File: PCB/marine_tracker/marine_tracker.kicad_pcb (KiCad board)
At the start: 4 copper layers, 83.7 x 40.3 mm, 59 parts, among them J1 Screw_Terminal_01x02, J2 Conn_ARM_JTAG_SWD_10, J3 USB_C_Receptacle_USB2.0_16P, J4 BM04B-GHS-TBT, J5 Conn_01x08_Pin, J6 Conn_Coaxial, SW1 SW_Push, U1 STM32U575RGT6, U2 SHT40, U3 MCP73833-xxx-UN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

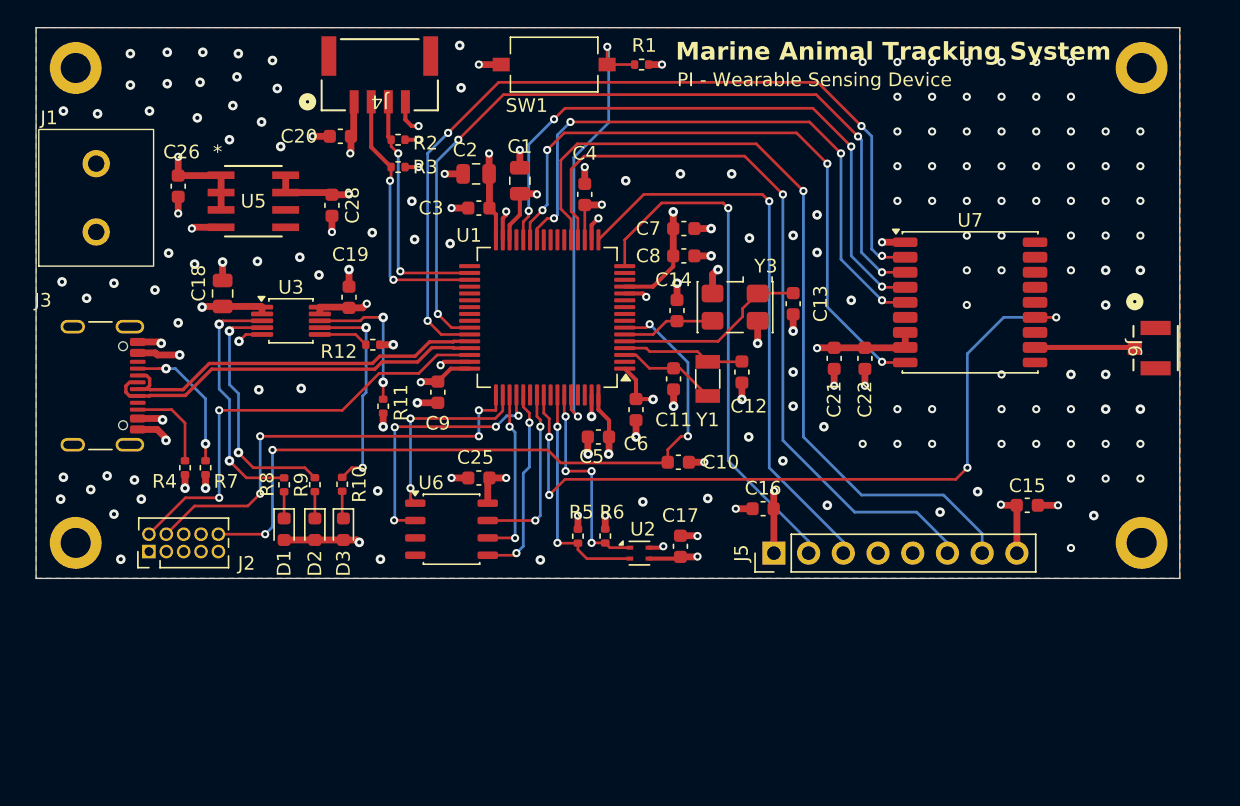
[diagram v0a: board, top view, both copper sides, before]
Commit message: drc violation PCB corrected
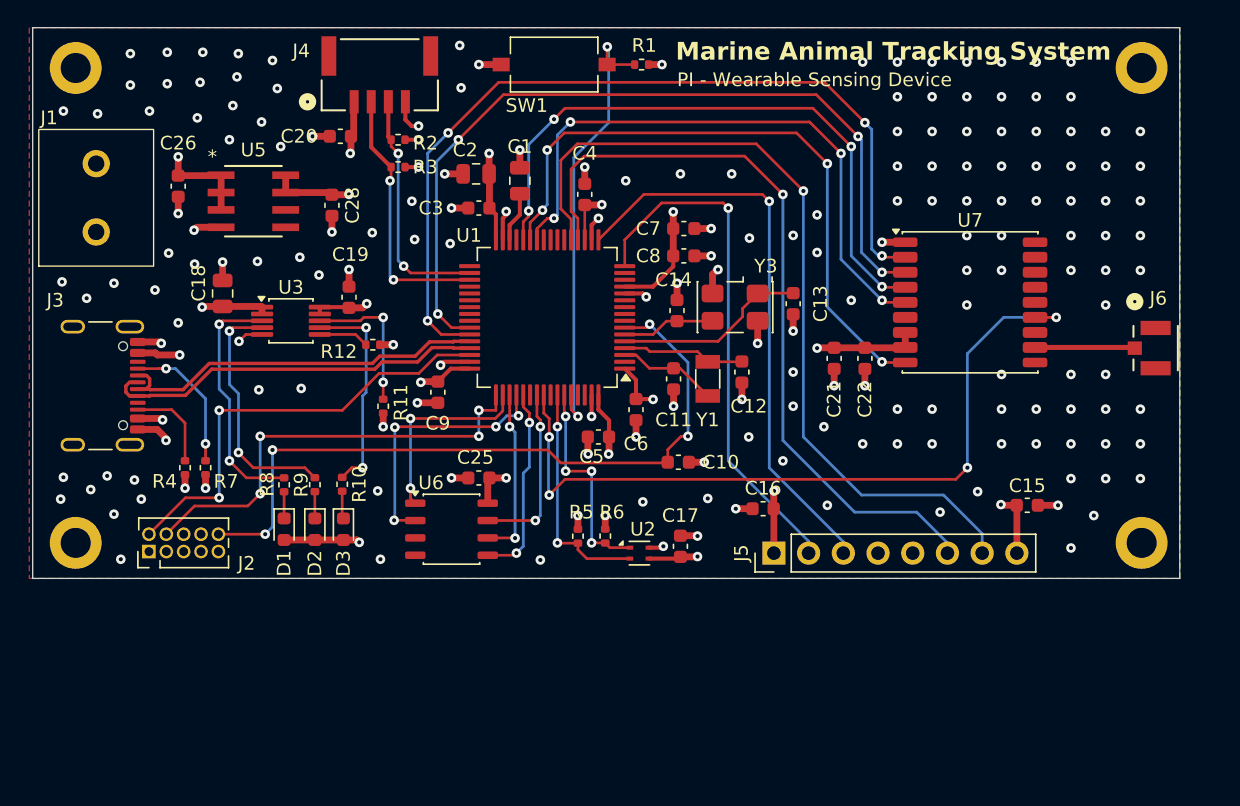
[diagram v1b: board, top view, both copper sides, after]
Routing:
- net /VCAP: track 4.96 -> 3.69 mm, vias 1 -> 0
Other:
- board size 83.7 x 40.3 mm -> 83.9 x 40.3 mm

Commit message: add reference to symbols
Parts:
- removed SW1: SW_Push, Button_Switch_SMD:SW_Tactile_SPST_NO_Straight_CK_PTS636Sx25SMTRLFS
- added SW2: SW_Push, Beuns_PCBFootprint:SW4_PTS815 SJM 250 SMTR LFS_CNK_btnPoussoir, F.Cu at (50.5, 67.8)
- moved R1 27.9 mm to (55.0, 67.2), turned to -90 degrees
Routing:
- net /BOOT0: track 33.4 -> 58.8 mm, vias 2 -> 4
- net +3V3: track 70.4 -> 75.1 mm
- net GND: track 62.6 -> 62.7 mm, vias 181 -> 207

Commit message: correction PCB
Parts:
- added C23: 1n, Capacitor_SMD:C_0603_1608Metric, F.Cu at (58.0, 78.8)
- added C24: 10u, Capacitor_SMD:C_0805_2012Metric, F.Cu at (114.0, 98.8)
- added C27: 10u, Capacitor_SMD:C_0805_2012Metric, F.Cu at (87.0, 99.5)
- added C29: 10u, Capacitor_SMD:C_0805_2012Metric, F.Cu at (102.0, 118.5)
- added C30: 10u, Capacitor_SMD:C_0805_2012Metric, F.Cu at (61.0, 74.5)
- R12: value 1k -> 2k
- U3: footprint Package_SO:MSOP-10_3x3mm_P0.5mm -> Beuns_PCBFootprint:lipo_charger
- U5: footprint Beuns_PCBFootprint:SOIC8-N_MC_MCH -> Beuns_PCBFootprint:LDO_1A
- moved C28 4.28 mm to (57.2, 74.2), turned to 180 degrees
- moved C16 2.30 mm to (89.5, 99.5), turned to 90 degrees
- moved C26 1.65 mm to (49.0, 74.2), turned to 0 degrees
- moved U5 1.38 mm to (53.1, 77.0)
- moved C19 1.30 mm to (61.2, 82.8), turned to 180 degrees
- moved C17 1.25 mm to (86.5, 103.2), turned to 0 degrees
- moved C18 1.03 mm to (52.5, 82.8), turned to 0 degrees
- moved C15 0.63 mm to (110.8, 98.8), turned to 90 degrees
- moved J1 0.25 mm to (42.8, 79.2)
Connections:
- U5 pad 6: unconnected-(U5-CDELAY-Pad6) -> Net-(U5-CDELAY)
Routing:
- net +3V3: track 75.1 -> 55.0 mm, vias 18 -> 29
- net +BATT: track 11.1 -> 0.00 mm, vias 2 -> 7
- net /BOOT0: track 58.8 -> 50.6 mm
- net VBUS: track 15.4 -> 10.6 mm, vias 4 -> 6
- net Net-(U5-CDELAY): track 0.00 -> 3.65 mm
- net /PG: track 15.5 -> 16.6 mm
- net /STAT2: track 18.0 -> 18.7 mm
- net /PROG: track 3.68 -> 4.39 mm
- net /THERM: track 10.7 -> 11.4 mm
- net /STAT1: track 18.3 -> 19.0 mm
- net GND: track 62.7 -> 63.0 mm, vias 207 -> 125
- added copper zone on F.Cu, net +3V3
- added copper zone on F.Cu, net +BATT
- added copper zone on F.Cu, net VBUS

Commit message: PCB finish
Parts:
- moved REF** 77.9 mm to (119.4, 101.6)
- moved REF** 77.6 mm to (41.9, 101.6)
- moved C29 24.8 mm to (98.2, 94.0), turned to 180 degrees
- moved C21 3.57 mm to (98.5, 91.8), turned to 180 degrees
- moved C22 1.46 mm to (98.5, 89.8), turned to 180 degrees
- moved REF** 0.41 mm to (41.9, 67.3)
- moved REF** 0.13 mm to (119.4, 67.3)
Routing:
- net +3V3: track 55.0 -> 58.7 mm
- net GND: track 63.0 -> 64.3 mm, vias 125 -> 118
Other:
- board text added: "+"
- board text added: "-"
- board text added: "3V3"
- board text added: "GND"
- board text added: "RX"
- board text added: "SCL"
- board text added: "SDA"
- board text added: "TX"
- board text added: "VPA_EN"
- board text added: "VPA_SEL"
